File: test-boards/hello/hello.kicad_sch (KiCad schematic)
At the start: 1 part, among them J1 Conn_01x02_Pin

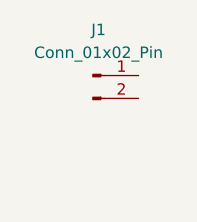
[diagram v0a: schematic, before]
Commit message: hello test board with components on both sides
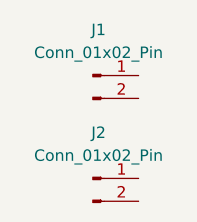
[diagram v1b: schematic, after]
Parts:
- added J2: Conn_01x02_Pin, Connector_PinHeader_2.54mm:PinHeader_1x02_P2.54mm_Vertical, symbol Connector:Conn_01x02_Pin
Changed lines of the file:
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@@
+	(symbol
+		(lib_id "Connector:Conn_01x02_Pin")
+		(at 124.46 87.63 0)
+		(unit 1)
+		(exclude_from_sim no)
+		(in_bom yes)
+		(on_board yes)
+		(dnp no)
+		(fields_autoplaced yes)
+		(property "Reference" "J2"
+			(at 125.095 82.55 0)
+			(effects
+				(font
+					(size 1.27 1.27)
+				)
+			)
+		)
+		(property "Value" "Conn_01x02_Pin"
+			(at 125.095 85.09 0)
+			(effects
+				(font
+					(size 1.27 1.27)
+				)
+			)
+		)
+		(property "Footprint" "Connector_PinHeader_2.54mm:PinHeader_1x02_P2.54mm_Vertical"
+			(at 124.46 87.63 0)
+			(effects
+				(font
+					(size 1.27 1.27)
+				)
+				(hide yes)
+			)
+		)
+		(property "Datasheet" "~"
+			(at 124.46 87.63 0)
+			(effects
+				(font
+					(size 1.27 1.27)
+				)
+				(hide yes)
+			)
+		)
+		(property "Description" "Generic connector, single row, 01x02, script generated"
+			(at 124.46 87.63 0)
+			(effects
+				(font
+					(size 1.27 1.27)
+				)
+				(hide yes)
+			)
+		)
+		(pin "2"
+		)
+		(pin "1"
+		)
+		(instances
+			(project "hello"
+				(path "/5b9556ff-85f4-45b0-a95e-eca15e761b94"
+					(reference "J2")
+					(unit 1)
+				)
+			)
+		)
+	)
 	(symbol
 		(lib_id "Connector:Conn_01x02_Pin")
